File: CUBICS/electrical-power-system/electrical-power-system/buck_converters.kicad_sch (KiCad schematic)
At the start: 42 parts, among them Q201 NMOS, U104 INA180, U201 LT1762-5

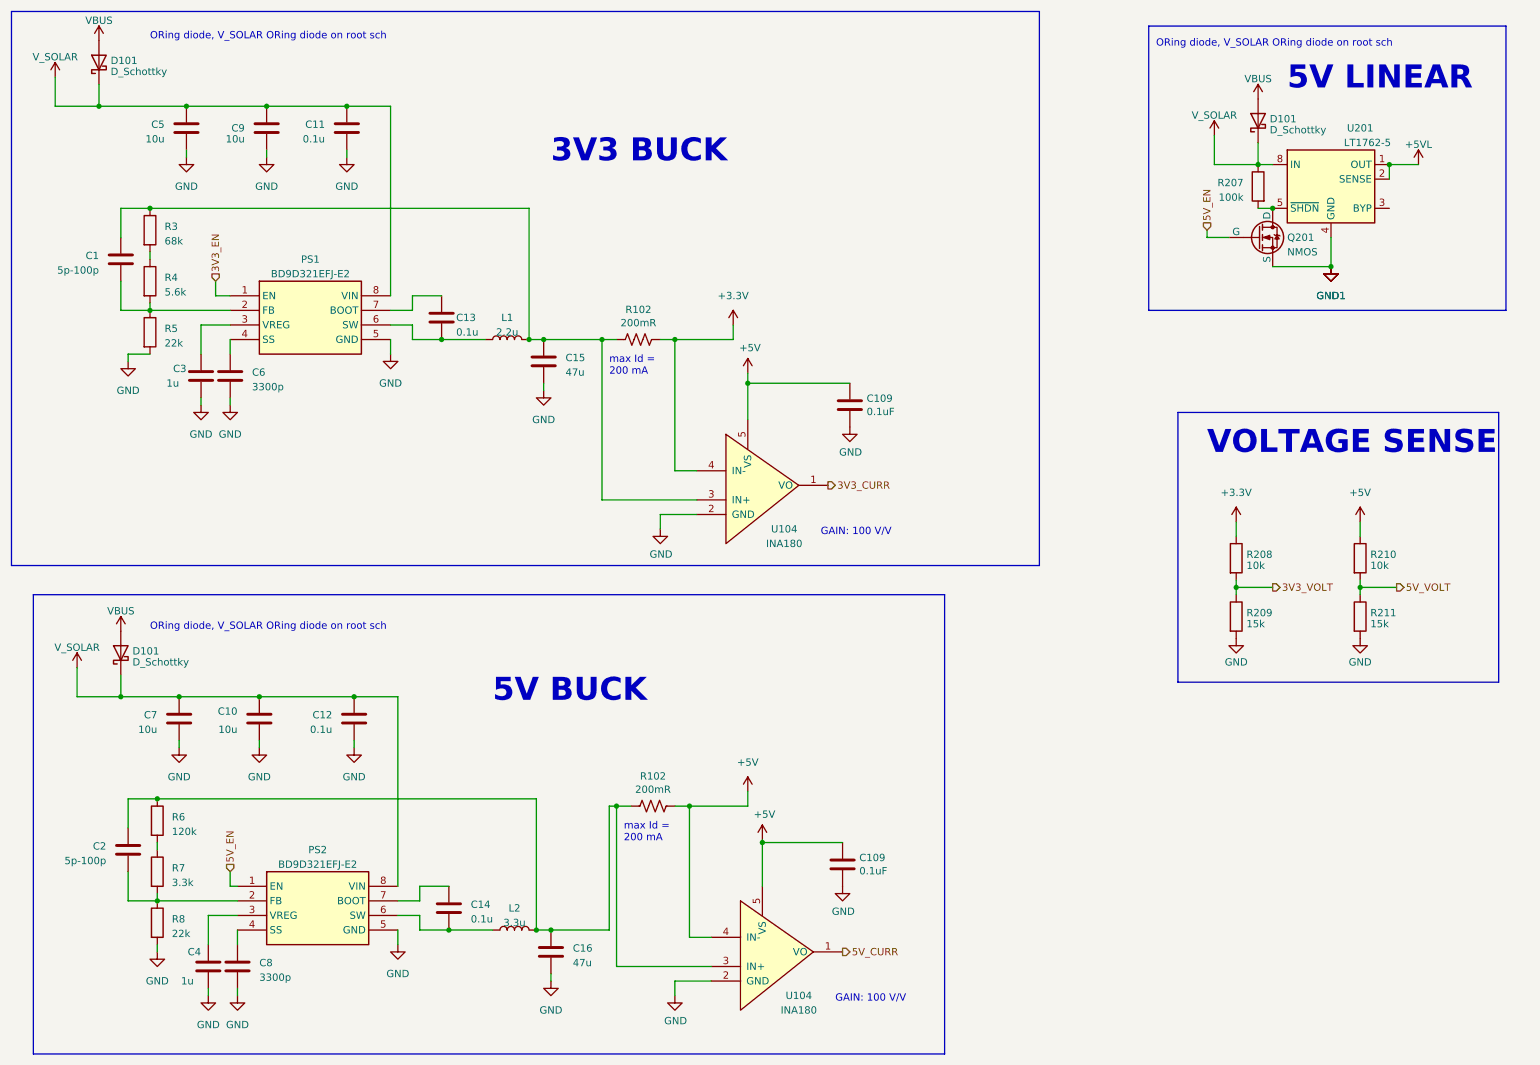
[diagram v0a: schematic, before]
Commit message: rev 1.0 routing complete updated schematic
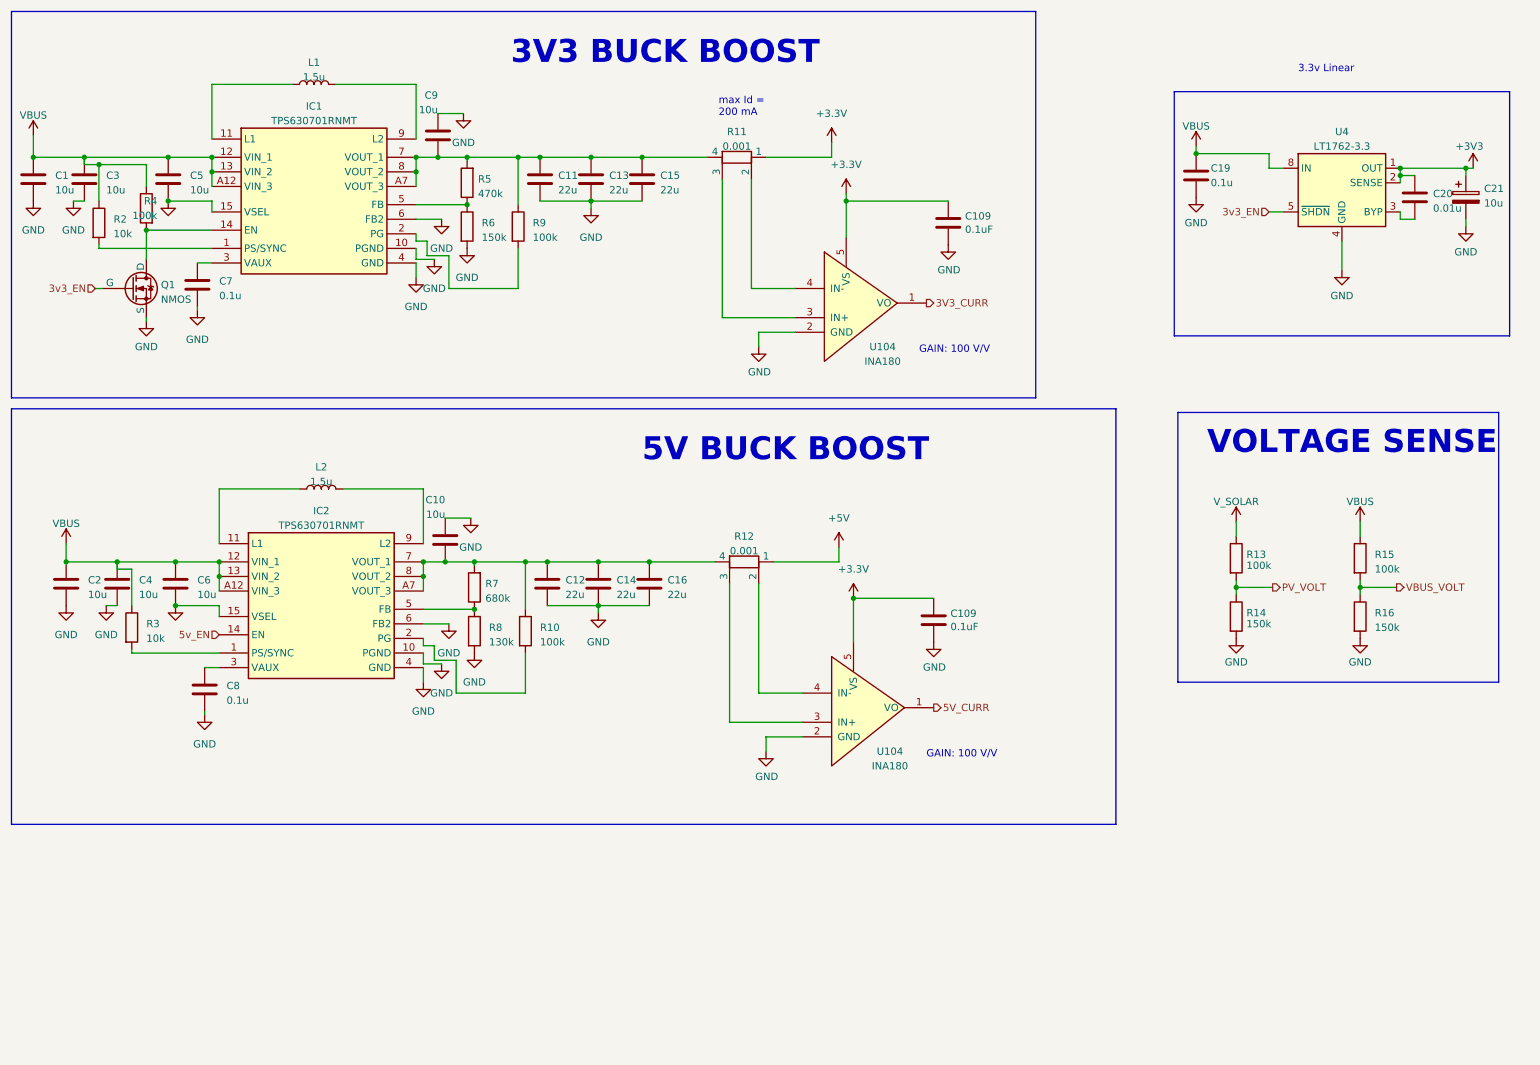
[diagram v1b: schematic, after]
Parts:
- removed D101 (x3): D_Schottky, symbol Device:D_Schottky
- removed PS1, PS2: BD9D321EFJ-E2, SamacSys_Parts:SOIC127P600X100-8N, symbol SamacSys_Parts:BD9D321EFJ-E2
- removed Q201: NMOS, Package_TO_SOT_SMD:SOT-23-3, symbol Simulation_SPICE:NMOS
- removed R102 (x2): 200mR, Resistor_SMD:R_0805_2012Metric_Pad1.20x1.40mm_HandSolder, symbol Device:R_US
- removed R207: 100k, Resistor_SMD:R_0603_1608Metric, symbol Device:R
- removed U201: LT1762-5, Package_SO:MSOP-8_3x3mm_P0.65mm, symbol Regulator_Linear:LT1762-5
- added C19: 0.1u, Capacitor_SMD:C_0603_1608Metric, symbol Device:C
- added C20: 0.01u, Capacitor_SMD:C_0402_1005Metric, symbol Device:C
- added C21: 10u, Capacitor_THT:CP_Radial_D4.0mm_P1.50mm, symbol Device:C_Polarized
- added IC1, IC2: TPS630701RNMT, SamacSys_Parts:TPS630701RNMT, symbol SamacSys_Parts:TPS630701RNMT
- added Q1: NMOS, Package_TO_SOT_SMD:SOT-23-3, symbol Simulation_SPICE:NMOS
- added R10, R9: 100k, Resistor_SMD:R_0603_1608Metric, symbol Device:R
- added R11, R12: 0.001, SamacSys_Parts:WSL27261L000FEA, symbol Device:R_Shunt
- added R2: 10k, Resistor_SMD:R_0603_1608Metric, symbol Device:R
- added U4: LT1762-3.3, Package_SO:MSOP-8_3x3mm_P0.65mm, symbol Regulator_Linear:LT1762-3.3
- C1, C2: value 5p-100p -> 10u; footprint Capacitor_SMD:C_0603_1608Metric -> Capacitor_SMD:C_0805_2012Metric
- C109: footprint Capacitor_SMD:C_0805_2012Metric_Pad1.18x1.45mm_HandSolder -> Capacitor_SMD:C_0603_1608Metric
- C11, C12, C13, C14: value 0.1u -> 22u; footprint Capacitor_SMD:C_0603_1608Metric -> Capacitor_SMD:C_0805_2012Metric
- C15, C16: value 47u -> 22u; footprint Capacitor_SMD:C_2220_5650Metric -> Capacitor_SMD:C_0805_2012Metric
- C3, C4: value 1u -> 10u; footprint Capacitor_SMD:C_0603_1608Metric -> Capacitor_SMD:C_0805_2012Metric
- C6: value 3300p -> 10u
- C7: value 10u -> 0.1u; footprint Capacitor_SMD:C_0603_1608Metric -> Capacitor_SMD:C_0402_1005Metric
- C8: value 3300p -> 0.1u; footprint Capacitor_SMD:C_0603_1608Metric -> Capacitor_SMD:C_0402_1005Metric
- L1: value 2.2u -> 1.5u; footprint Inductor_SMD:L_12x12mm_H6mm -> Inductor_SMD:L_Bourns-SRN4018
- L2: value 3.3u -> 1.5u; footprint Inductor_SMD:L_12x12mm_H6mm -> Inductor_SMD:L_Bourns-SRN4018
- R13: renamed from R208; value 10k -> 100k; footprint (none) -> Resistor_SMD:R_0603_1608Metric
- R14: renamed from R209; value 15k -> 150k; footprint (none) -> Resistor_SMD:R_0603_1608Metric
- R15: renamed from R210; value 10k -> 100k; footprint (none) -> Resistor_SMD:R_0603_1608Metric
- R16: renamed from R211; value 15k -> 150k; footprint (none) -> Resistor_SMD:R_0603_1608Metric
- R3: value 68k -> 10k
- R4: value 5.6k -> 100k
- R5: value 22k -> 470k
- R6: value 120k -> 150k
- R7: value 3.3k -> 680k
- R8: value 22k -> 130k
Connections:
- net +1V2: now also R13.1; no longer C10.1, C11.1, C12.1, C5.1, C7.1, C9.1
- net +3.3V: now also C109.1, C109.1, U104.5 (VS), U104.5 (VS), R11.1; no longer R13.1, U104.4 (IN-)
- net +5V: now also R12.1; no longer C109.1, C109.1, R15.1, U104.4 (IN-), U104.5 (VS), U104.5 (VS)
- net GND: now also C1.2, C13.2, C14.2, C2.2, R6.2, C19.2, C21.2, IC1.10 (PGND), IC1.15 (VSEL), IC1.4 (GND), IC1.6 (FB2), IC2.10 (PGND), IC2.15 (VSEL), IC2.4 (GND), IC2.6 (FB2), Q1.3 (S), U4.4 (GND); no longer R5.2
- net VBUS: now also C1.1, C2.1, C3.1, C4.1, C5.1, C6.1, R15.1, R3.1, R4.1, C19.1, IC1.12 (VIN_1), IC1.13 (VIN_2), IC1.A12 (VIN_3), IC2.12 (VIN_1), IC2.13 (VIN_2), IC2.A12 (VIN_3), R2.1, U4.8 (IN)
- net at R7.1: now also R8.1, IC2.5 (FB); no longer R6.2
- net at C14.1: now also C10.1, C12.1, C16.1, R7.2, IC2.7 (VOUT_1), IC2.8 (VOUT_2), IC2.A7 (VOUT_3), R10.1, R12.4
- net at L2.1: now also IC2.11 (L1); no longer C14.2
- net at C8.1: now also IC2.3 (VAUX)
- net at R3.2: now also IC2.1 (PS/SYNC); no longer R4.1
- net at C13.1: now also C11.1, C15.1, C9.1, R5.2, IC1.7 (VOUT_1), IC1.8 (VOUT_2), IC1.A7 (VOUT_3), R11.4, R9.1
- net at L1.1: now also IC1.11 (L1); no longer C13.2
- net 3V3_VOLT renamed PV_VOLT
- net 5V_VOLT renamed VBUS_VOLT
- new net: IC2.2 (PG), R10.2
- new net: IC2.9 (L2), L2.2
- new net: R11.2, U104.4 (IN-)
- new net: R11.3, U104.3 (IN+)
- new net: IC1.5 (FB), R5.1, R6.1
- new net: IC1.9 (L2), L1.2
- new net: R12.3, U104.3 (IN+)
- new net: R12.2, U104.4 (IN-)
- new net: C20.2, U4.3 (BYP)
- new net: IC1.14 (EN), Q1.1 (D), R4.2
- new net: IC1.1 (PS/SYNC), R2.2
- new net: IC1.2 (PG), R9.2
- new net: C7.1, IC1.3 (VAUX)
- new net +3V3: C20.1, C21.1, U4.1 (OUT), U4.2 (SENSE)
- new net 3v3_EN: Q1.2 (G), U4.5 (~{SHDN})
- new net 5v_EN: IC2.14 (EN)
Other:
- note added: "3.3v Linear"
- note added: "3V3 BUCK BOOST"
- note added: "5V BUCK BOOST"
- note removed: "3V3 BUCK"
- note removed: "5V BUCK"
- note removed: "5V LINEAR"
- note removed: "ORing diode, V_SOLAR ORing diode on root sch"
- moved on the sheet: C109, U104
